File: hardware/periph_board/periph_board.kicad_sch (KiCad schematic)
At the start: 25 parts, among them IC100 CD74HC4067SM96, IC101 LP2950-33LPRE3, IC102 ADC121S021CIMFX_NOPB, J100 2x10 Male Pins

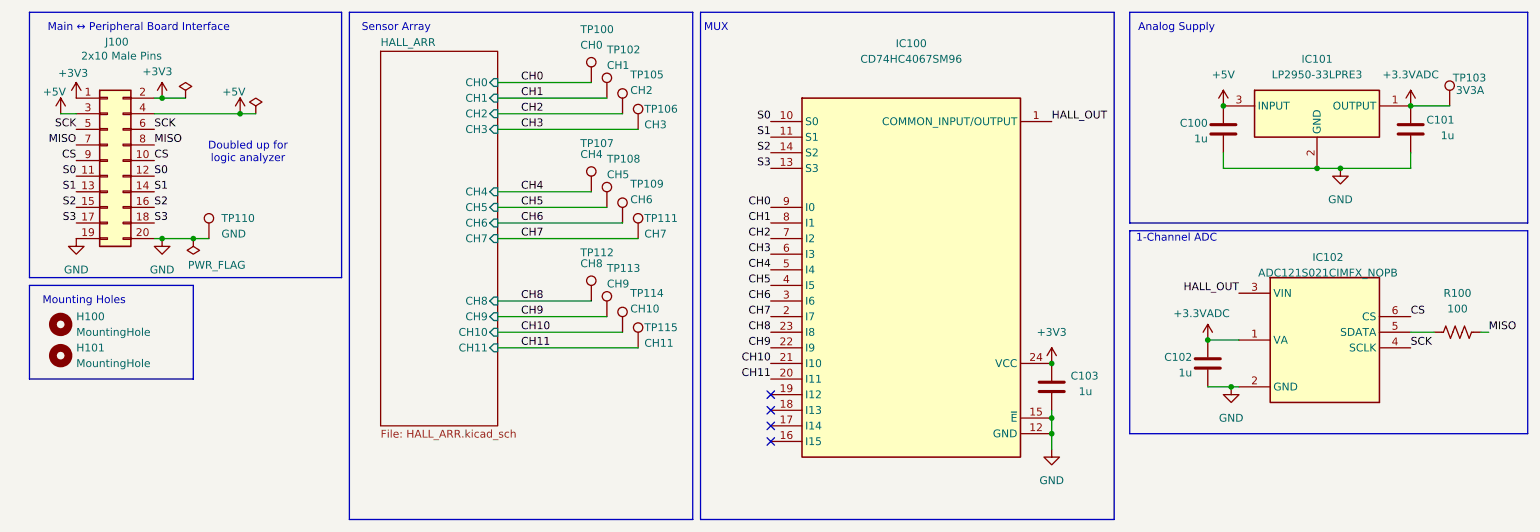
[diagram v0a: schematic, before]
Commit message: replaced LDO thing to be free one in lab checkout. added some stuff to main board (wip)
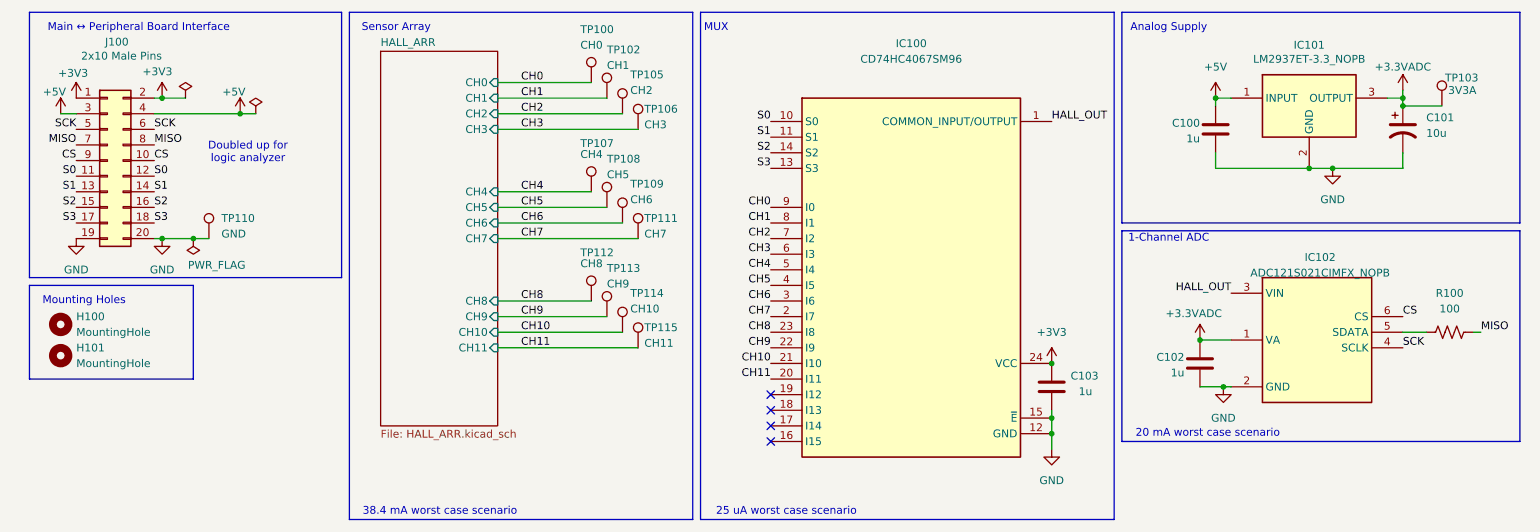
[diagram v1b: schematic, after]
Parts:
- removed C101: 1u, Capacitor_SMD:C_0805_2012Metric_Pad1.18x1.45mm_HandSolder, symbol Device:C
- removed IC101: LP2950-33LPRE3, 445L:TL431CLPM, symbol LP2950-33LPRE3:LP2950-33LPRE3
- added C101: 10u, Capacitor_SMD:C_0805_2012Metric, symbol Device:C_Polarized_US
- added IC101: LM2937ET-3.3_NOPB, 445L:TO254P470X1028X1955-3P, symbol ECE445L:LM2937ET-3.3_NOPB
- IC102: footprint SOT95P280X145-6N -> SamacSys_Parts:SOT95P280X145-6N
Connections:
- net +3.3VADC: now also C101.1, IC101.3 (OUTPUT)
- net +5V: now also IC101.1 (INPUT)
- net GND: now also C101.2, IC101.2 (GND)
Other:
- note added: "20 mA worst case scenario"
- note added: "25 uA worst case scenario"
- note added: "38.4 mA worst case scenario"
- moved on the sheet: C100, C102, IC102, R100, TP103
